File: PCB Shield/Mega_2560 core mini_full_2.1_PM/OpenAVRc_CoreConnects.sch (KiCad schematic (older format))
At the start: 19 parts, among them P1 2560-core, P10 RX1TX1, P15 DUMMY, P16 LCD, P6 Micro_sd, P9 SPI, Q1 IRLML5203

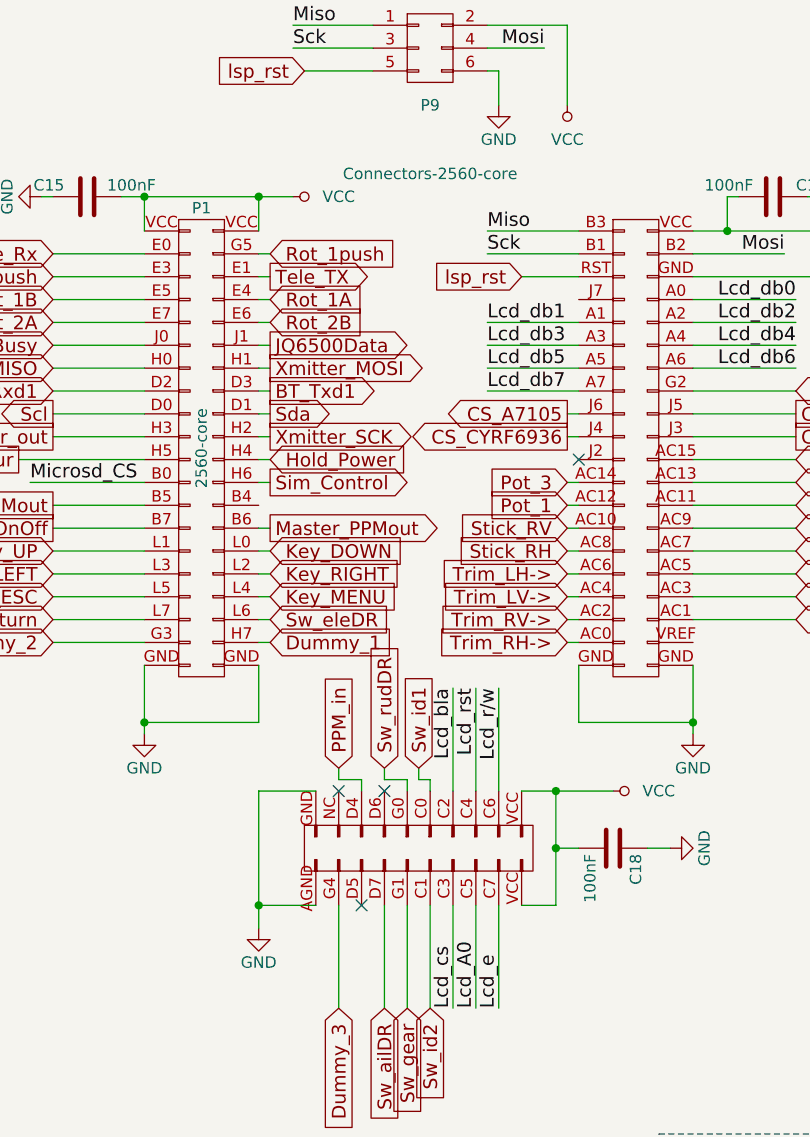
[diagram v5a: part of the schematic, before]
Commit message: Update pcb shield
Update core component (change pin 99 from GND to AGND).
Remove GND on AGND pin.
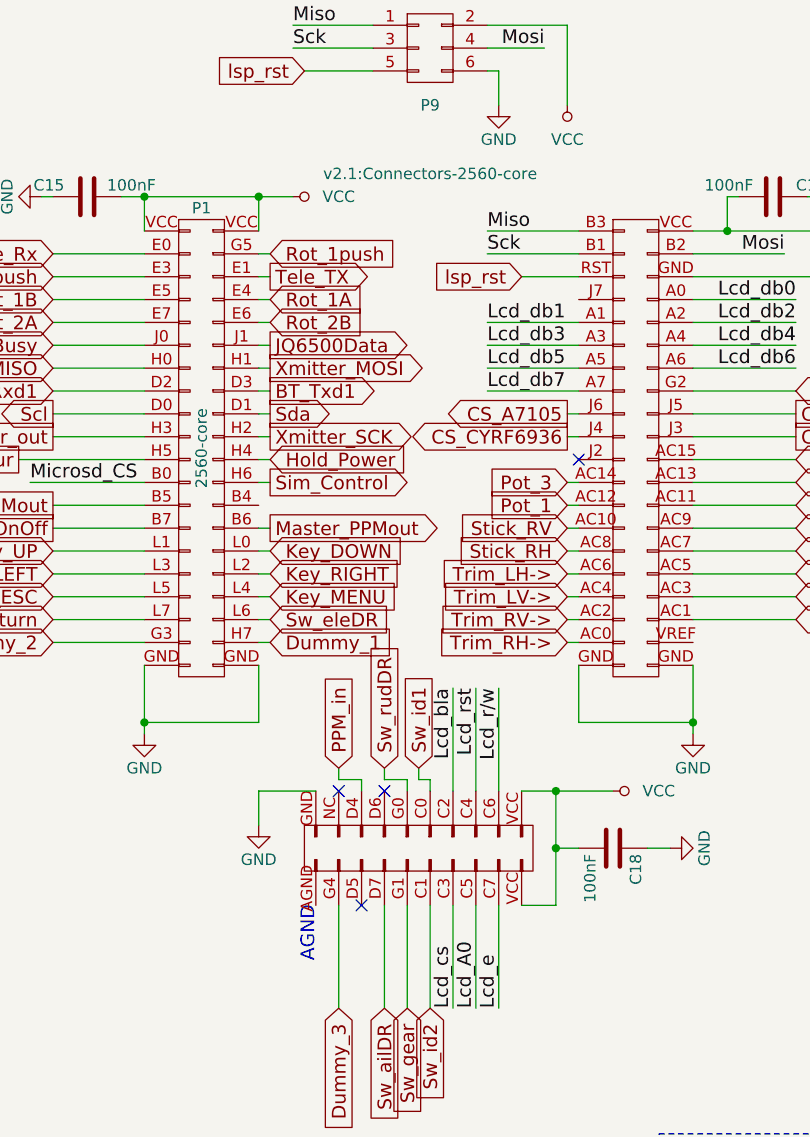
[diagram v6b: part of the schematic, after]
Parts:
- P1: footprint Connectors-2560-core -> v2.1:Connectors-2560-core
- P15: footprint (none) -> Pin_Headers:Pin_Header_Straight_1x03_Pitch2.54mm
- Q1: footprint SOT-23_MOS_P -> v2.1:SOT-23_MOS_P
- RV1, RV6: footprint trimpot_5x5_vertical -> v2.1:trimpot_5x5_vertical
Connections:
- net GND: no longer P1.AGND (P99)
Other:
- note added: "AGND"
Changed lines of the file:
@@
 Sheet 3 7
 Title "Shield Mega2560 core Full"
-Date "2018-04-19"
+Date "2018-04-25"
 Rev "2.10"
 Comp "© Team OpenAVRc"
@@
 L GND-RESCUE-Mega_2560_core_mini_full_2.0 #PWR053
 U 1 1 59C5DE2D
-P 2350 5300
-F 0 "#PWR053" H 2350 5050 50  0001 C CNN
-F 1 "GND" H 2350 5150 50  0000 C CNN
-F 2 "" H 2350 5300 50  0000 C CNN
-F 3 "" H 2350 5300 50  0000 C CNN
-	1    2350 5300
+P 2350 4850
+F 0 "#PWR053" H 2350 4600 50  0001 C CNN
+F 1 "GND" H 2350 4700 50  0000 C CNN
+F 2 "" H 2350 4850 50  0000 C CNN
+F 3 "" H 2350 4850 50  0000 C CNN
+	1    2350 4850
 	1    0    0    -1
 $EndComp
@@
 F 0 "RV6" V 10100 2700 50  0000 C CNN
 F 1 "1K" V 10200 2700 50  0000 C CNN
-F 2 "trimpot_5x5_vertical" H 10200 2700 50  0001 C CNN
+F 2 "v2.1:trimpot_5x5_vertical" H 10200 2700 50  0001 C CNN
 F 3 "" H 10200 2700 50  0000 C CNN
 	1    10200 2700
@@
 F 0 "RV1" V 9050 2400 50  0000 C CNN
 F 1 "10K" V 9150 2400 50  0000 C CNN
-F 2 "trimpot_5x5_vertical" H 9150 2400 50  0001 C CNN
+F 2 "v2.1:trimpot_5x5_vertical" H 9150 2400 50  0001 C CNN
 F 3 "" H 9150 2400 50  0000 C CNN
 	1    9150 2400
@@
 F 0 "Q1" V 9000 5000 60  0000 R CNN
 F 1 "IRLML5203" V 9300 5050 60  0000 R CNN
-F 2 "SOT-23_MOS_P" H 9100 4800 60  0001 C CNN
+F 2 "v2.1:SOT-23_MOS_P" H 9100 4800 60  0001 C CNN
 F 3 "" H 9100 4800 60  0000 C CNN
 	1    9100 4800
@@
 	1    0    0    -1
 $EndComp
-$Comp
-L 2560-core-RESCUE-Mega_2560_core_mini_full_2.1 P1
-U 1 1 5A758C27
-P 50 3400
-AR Path="/5A758C27" Ref="P1"  Part="1"
-AR Path="/59C5D60D/5A758C27" Ref="P1"  Part="1"
-F 0 "P1" H 2100 4650 50  0000 C CNN
-F 1 "2560-core" V 2100 3600 50  0000 C CNN
-F 2 "Connectors-2560-core" H 3100 4800 50  0000 C CNN
-F 3 "" H 2100 2650 50  0000 C CNN
-	1    50   3400
-	1    0    0    -1
-$EndComp
 Text GLabel 1450 3550 0    60   Output ~ 0
 BT_OnOff
@@
 F 0 "P15" H 4350 6850 50  0000 C CNN
 F 1 "DUMMY" V 4450 6650 50  0000 C CNN
-F 2 "" H 4350 6650 50  0000 C CNN
+F 2 "Pin_Headers:Pin_Header_Straight_1x03_Pitch2.54mm" H 4350 6650 50  0001 C CNN
 F 3 "" H 4350 6650 50  0000 C CNN
 	1    4350 6650
@@
 	2600 4700 2350 4700
 Wire Wire Line
-	2350 4700 2350 5300
-Wire Wire Line
-	2600 5200 2350 5200
-Connection ~ 2350 5200
+	2350 4700 2350 4850
 Wire Wire Line
 	1850 4400 2350 4400
@@
 Wire Notes Line
 	4100 7000 4100 6200
+Text Notes 2600 5450 1    60   ~ 0
+AGND
+$Comp
+L 2560-core-RESCUE-Mega_2560_core_mini_full_2.1 P1
+U 1 1 5A758C27
+P 50 3400
+AR Path="/5A758C27" Ref="P1"  Part="1"
+AR Path="/59C5D60D/5A758C27" Ref="P1"  Part="1"
+F 0 "P1" H 2100 4650 50  0000 C CNN
+F 1 "2560-core" V 2100 3600 50  0000 C CNN
+F 2 "v2.1:Connectors-2560-core" H 3100 4800 50  0000 C CNN
+F 3 "" H 2100 2650 50  0000 C CNN
+	1    50   3400
+	1    0    0    -1
+$EndComp
 $EndSCHEMATC
